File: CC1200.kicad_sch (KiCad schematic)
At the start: 36 parts, among them P1 AntMount, U3 CC1200, X1 40MHz

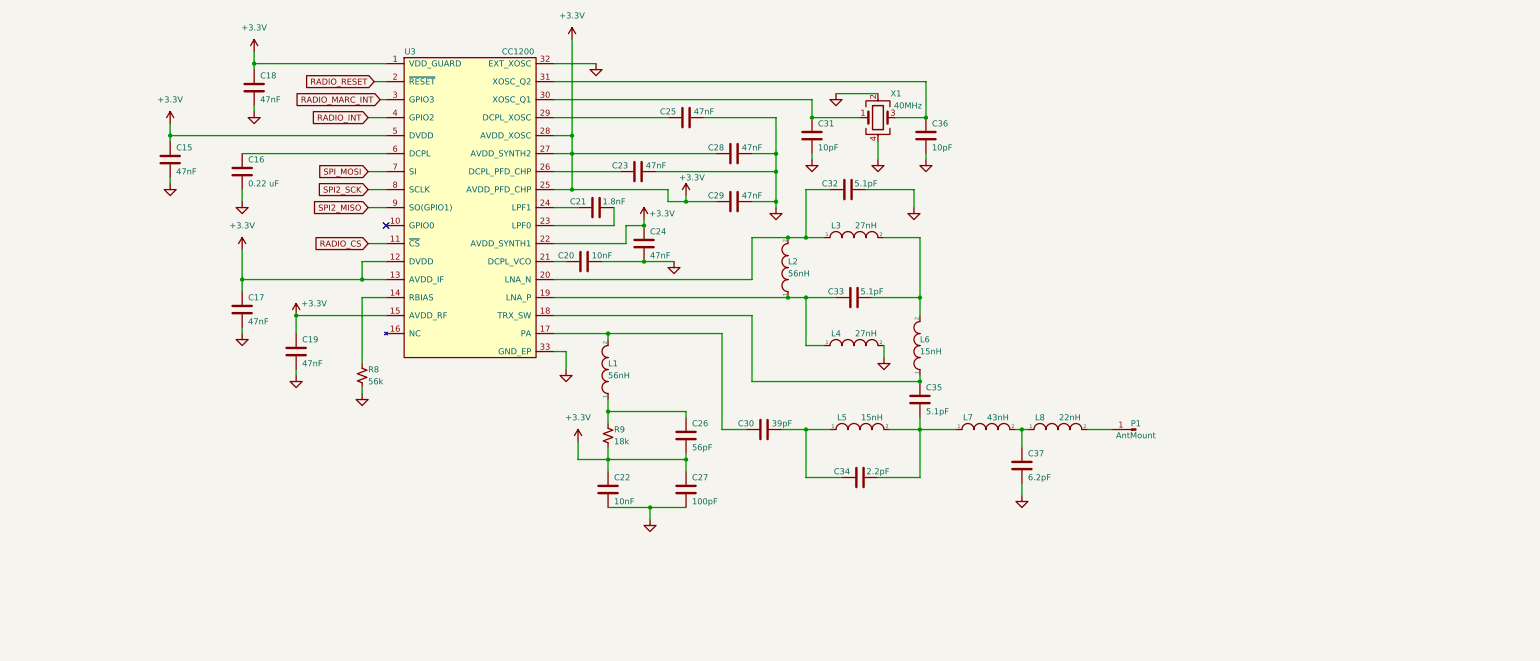
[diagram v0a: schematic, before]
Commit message: V4 Changes Added SKYWORKS +30db 4W FEM Added LM2576 3.9V supply Increased diameter to 60mm Re-routed full board
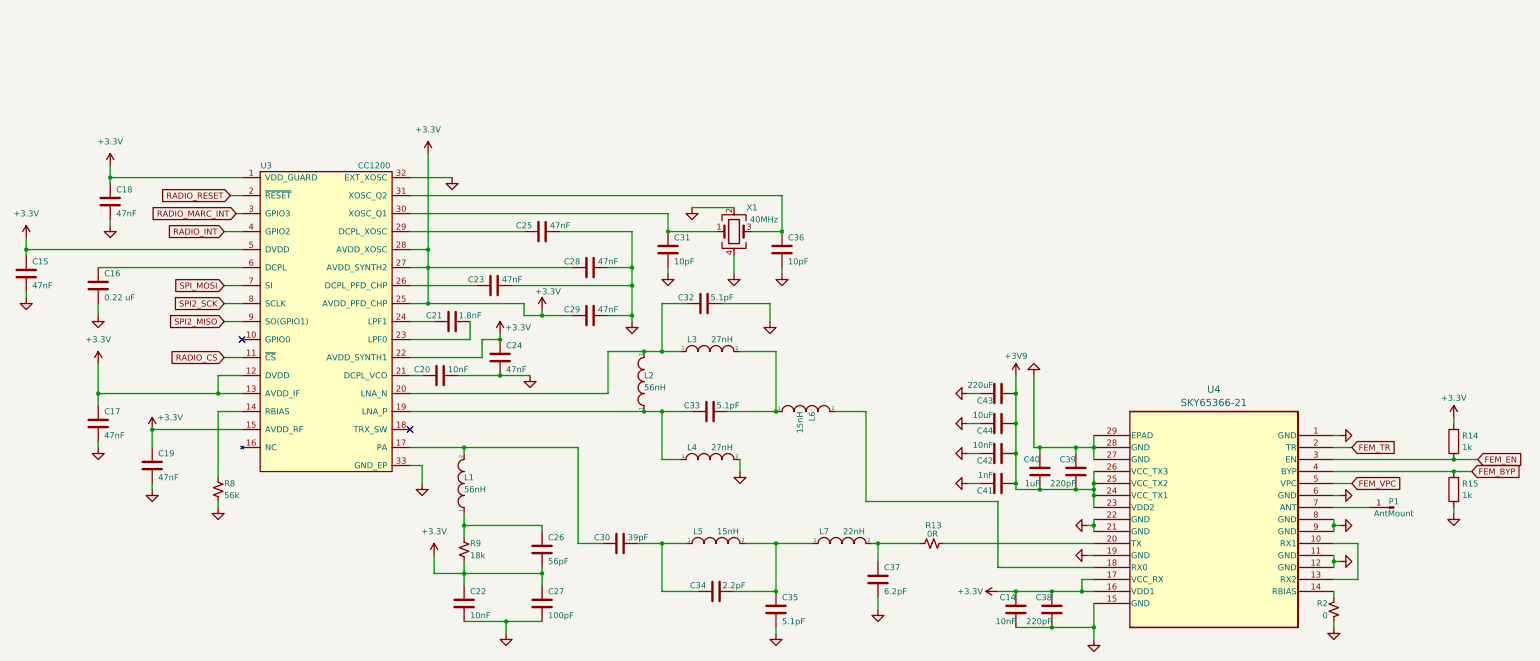
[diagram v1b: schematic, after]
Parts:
- removed L8: 22nH, Capacitor_SMD:C_0402_1005Metric, symbol pspice:INDUCTOR
- added C14, C42: 10nF, Capacitor_SMD:C_0402_1005Metric, symbol Device:C
- added C38, C39: 220pF, Capacitor_SMD:C_0402_1005Metric, symbol Device:C
- added C40: 1uF, Capacitor_SMD:C_0402_1005Metric, symbol Device:C
- added C41: 1nF, Capacitor_SMD:C_0402_1005Metric, symbol Device:C
- added C43: 220uF, Capacitor_SMD:C_1206_3216Metric, symbol Device:C
- added C44: 10uF, Capacitor_SMD:C_0402_1005Metric, symbol Device:C
- added R13: 0R, Capacitor_SMD:C_0402_1005Metric, symbol Device:R_Small_US
- added R14, R15: 1k, Resistor_SMD:R_0402_1005Metric, symbol Device:R
- added R2: 0, Capacitor_SMD:C_0402_1005Metric, symbol Device:R_Small_US
- added U4: SKY65366-21, SKY65366:SKY65366-21_SKY, symbol 2024-09-25_23-00-01:SKY65366-21
- L7: value 43nH -> 22nH; LCSC Part C2042359 -> C12670
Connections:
- net +3.3V: now also C14.1, C38.1, R14.2, U4.16 (VDD1), U4.17 (VCC_RX)
- net GND: now also C35.2, C14.2, C38.2, C39.1, C40.1, C41.1, C42.1, C43.1, C44.1, R15.1, R2.2, U4.1 (GND), U4.11 (GND), U4.12 (GND), U4.15 (GND), U4.19 (GND), U4.21 (GND), U4.22 (GND), U4.27 (GND), U4.28 (GND), U4.29 (EPAD), U4.6 (GND), U4.8 (GND), U4.9 (GND)
- net at C37.1, L7.2: now also R13.1
- net at P1.1 (Pin_1): now also U4.7 (ANT)
- net at C33.1, L3.2: now also L6.1; no longer L6.2
- net at C34.1, L5.2, L7.1: now also C35.1; no longer C35.2
- new net: R2.1, U4.14 (RBIAS)
- new net: R13.2, U4.20 (TX)
- new net: L6.2, U4.18 (RX0)
- new net: U4.10 (RX1), U4.13 (RX2)
- new net +3V9: C39.2, C40.2, C41.2, C42.2, C43.2, C44.2, U4.23 (VDD2), U4.24 (VCC_TX1), U4.25 (VCC_TX2), U4.26 (VCC_TX3)
- new net FEM_BYP: R15.2, U4.4 (BYP)
- new net FEM_EN: R14.1, U4.3 (EN)
- new net FEM_TR: U4.2 (TR)
- new net FEM_VPC: U4.5 (VPC)
- now unconnected: U3.18 (TRX_SW)
- no-connect marks 1 -> 2
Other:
- moved on the sheet: C15, C16, C17, C18, C19, C20, C21, C22, C23, C24, C25, C26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

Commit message: Adjusted some component footprints and part numbers Increased size of inductor and repositioned generated gbrs, drills, bom and cpl (up to date)
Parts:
- C21: LCSC Part C152808 -> C162192
- L1, L2: LCSC Part C76777 -> C167484
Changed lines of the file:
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@@
 			)
 		)
-		(property "LCSC Part" "C152808"
+		(property "LCSC Part" "C162192"
 			(at 109.22 101.6 0)
 			(effects
@@
 			)
 		)
-		(property "LCSC Part" "C76777"
+		(property "LCSC Part" "C167484"
 			(at 111.76 135.89 0)
 			(effects
@@
 			)
 		)
-		(property "LCSC Part" "C76777"
+		(property "LCSC Part" "C167484"
 			(at 149.86 114.3 0)
 			(effects

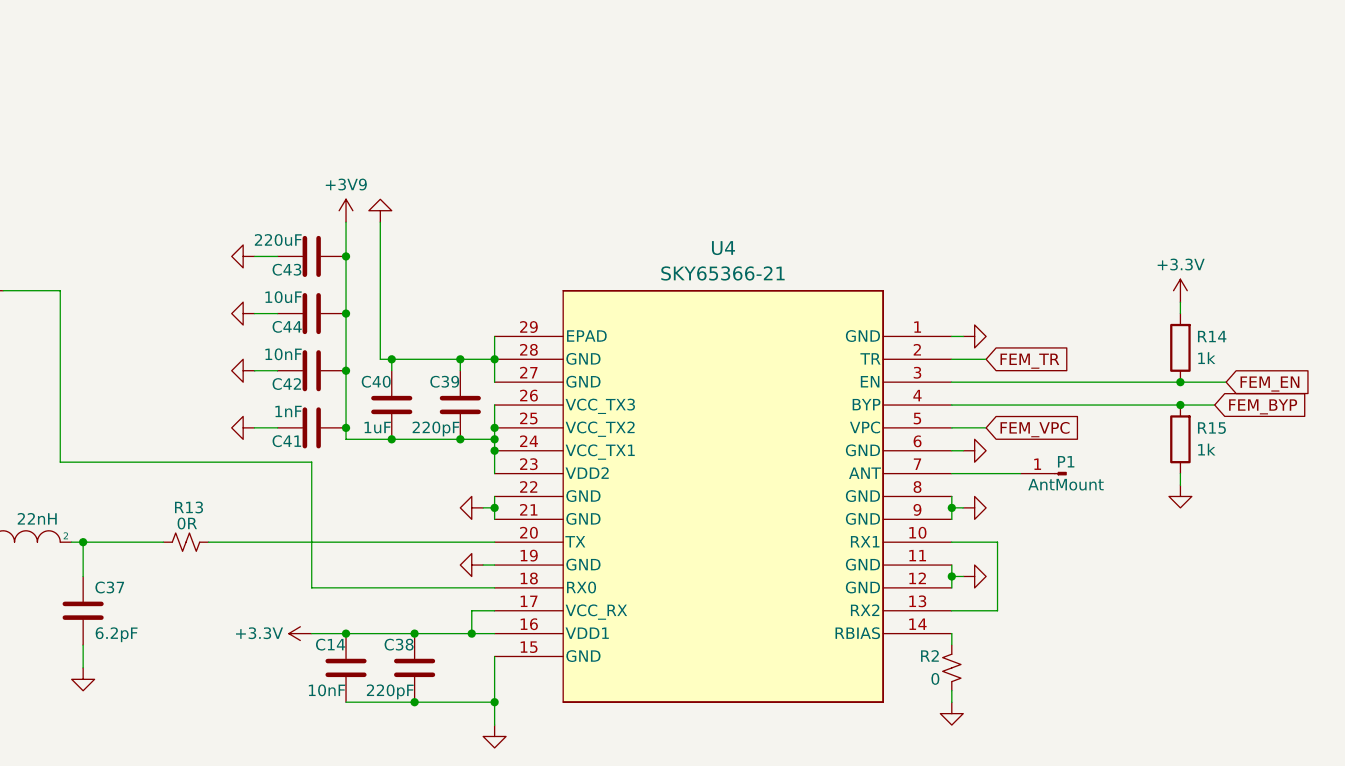
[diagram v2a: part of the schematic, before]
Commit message: removed old PA
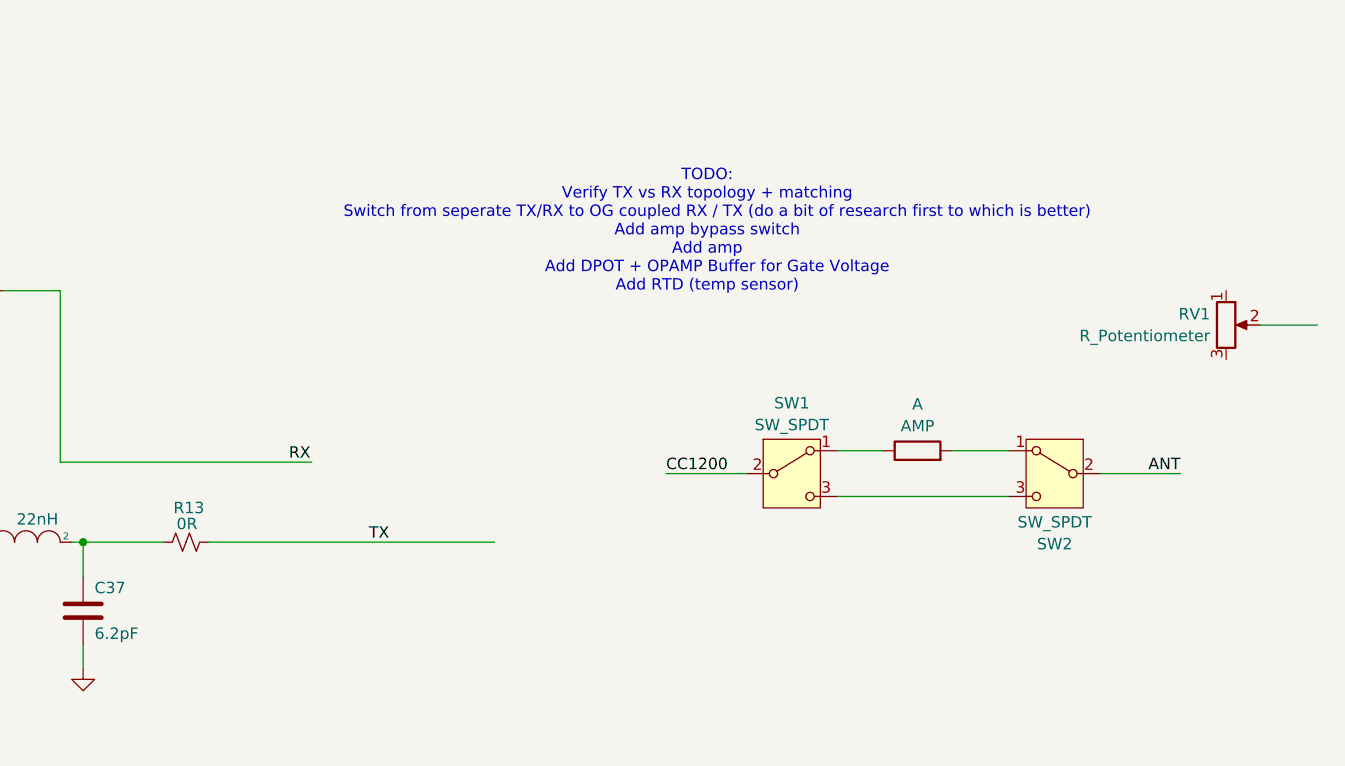
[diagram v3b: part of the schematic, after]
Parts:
- removed C14, C42: 10nF, Capacitor_SMD:C_0402_1005Metric, symbol Device:C
- removed C38, C39: 220pF, Capacitor_SMD:C_0402_1005Metric, symbol Device:C
- removed C40: 1uF, Capacitor_SMD:C_0402_1005Metric, symbol Device:C
- removed C41: 1nF, Capacitor_SMD:C_0402_1005Metric, symbol Device:C
- removed C43: 220uF, Capacitor_SMD:C_1206_3216Metric, symbol Device:C
- removed C44: 10uF, Capacitor_SMD:C_0402_1005Metric, symbol Device:C
- removed P1: AntMount, Connector_Coaxial:SMA_Amphenol_132134-11_Vertical, symbol Connector:Conn_01x01_Male
- removed R14, R15: 1k, Resistor_SMD:R_0402_1005Metric, symbol Device:R
- removed R2: 0, Capacitor_SMD:C_0402_1005Metric, symbol Device:R_Small_US
- removed U4: SKY65366-21, SKY65366:SKY65366-21_SKY, symbol 2024-09-25_23-00-01:SKY65366-21
- added A: AMP, symbol Device:R
- added RV1: R_Potentiometer, symbol Device:R_Potentiometer
- added SW1, SW2: SW_SPDT, symbol Switch:SW_SPDT
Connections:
- net TX: now reaches R13.2
- net RX: now reaches L6.2
- new net: A.1, SW1.1 (A)
- new net: SW1.3 (C), SW2.3 (C)
- new net: A.2, SW2.1 (A)
- new net ANT: SW2.2 (B)
- new net CC1200: SW1.2 (B)
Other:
- note added: "TODO: Verify TX vs RX topology + matching Switch from seperate TX/RX to OG coupled RX / TX (do a bit of research first to which is better) Add amp bypass switch Add amp Add DPOT + OPAMP Buffer for Gate Voltage Add RTD (temp sensor)"

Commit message: added Mitsibushi Amp w/ supporting gate control circuitry, switching, and temperature monitoring
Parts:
- removed A: AMP, symbol Device:R
- removed RV1: R_Potentiometer, symbol Device:R_Potentiometer
- removed SW1, SW2: SW_SPDT, symbol Switch:SW_SPDT
- added AE2: Antenna_Shield, Connector_Coaxial:SMA_Amphenol_132134-11_Vertical, symbol Device:Antenna_Shield
- added C67, C70, C71: 0.1uF, Capacitor_SMD:C_0402_1005Metric, symbol Device:C
- added C68, C72, C73: 100pF, Capacitor_SMD:C_0402_1005Metric, symbol Device:C
- added C69: 10nF, Capacitor_SMD:C_0402_1005Metric, symbol Device:C
- added JP3: SolderJumper_2_Bridged, Jumper:SolderJumper-2_P1.3mm_Bridged_RoundedPad1.0x1.5mm, symbol Jumper:SolderJumper_2_Bridged
- added JP4: SolderJumper_2_Open, Jumper:SolderJumper-2_P1.3mm_Open_RoundedPad1.0x1.5mm, symbol Jumper:SolderJumper_2_Open
- added L16: 43nH, Inductor_SMD:L_0402_1005Metric, symbol pspice:INDUCTOR
- added PE4259-63: 4259-63, Package_TO_SOT_SMD:SOT-363_SC-70-6, symbol 4259-63:4259-63
- added R17: 100, Resistor_SMD:R_0402_1005Metric, symbol Device:R_US
- added R18: 1000, Resistor_SMD:R_0402_1005Metric, symbol Device:R_US
- added R19: 1k, Resistor_SMD:R_0402_1005Metric, symbol Device:R_Small_US
- added RFAMP2: RA07H4047M-101, RA07H4047m:RA07h4047M, symbol RA07H4047M-101:RA07H4047M-101
- added TH1: PT100, Resistor_SMD:R_0603_1608Metric, symbol Sensor_Temperature:PT100
- added U7: MCP41010, MCP41010:SOIC127P599X175-8N, symbol Potentiometer_Digital:MCP41010
- added U8: MCP6001-OT, Package_TO_SOT_SMD:SOT-23-5, symbol Amplifier_Operational:MCP6001-OT
- R9: value 18k -> 18; footprint Capacitor_SMD:C_0402_1005Metric -> Resistor_SMD:R_0402_1005Metric
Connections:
- net RX is gone; now on an unnamed net: L6.2
- net +3.3V: now also C70.2, C71.1, PE4259-63.6 (~{CTRL_OR_VDD}), R19.2, TH1.2, U7.5 (PA0), U7.8 (VDD), U8.5 (V+)
- net GND: now also AE2.2 (Shield), C67.2, C69.1, C70.1, C71.2, PE4259-63.2 (GND), R17.2, RFAMP2.5 (GND), U7.4 (VSS), U7.7 (PB0), U8.2 (V-); no longer C35.2
- net at U3.18 (TRX_SW): now also C35.1
- net at C34.1, L5.2: now also C35.2, L16.2; no longer C35.1, L7.1
- net at L7.2, R13.1: no longer C37.1
- net TX: no longer names the net of R13.2
- net TX: now also C68.1
- new net: AE2.1 (A), C73.2, RFAMP2.4 (RF_OUTPUT_(POUT))
- new net: JP3.1 (A), U7.6 (PW0)
- new net: JP3.2 (B), JP4.1 (A), U8.3 (+)
- new net: R17.1, R18.1, TH1.1
- new net: C73.1, PE4259-63.1 (RF1)
- new net: C72.1, PE4259-63.3 (RF2)
- new net: C68.2, PE4259-63.5 (RFC)
- new net: C72.2, RFAMP2.1 (RF_INPUT_(PIN))
- new net: C37.1, L16.1, L7.1
- new net: RFAMP2.2 (GATE_VOLTAGE_(VGG)), U8.1, U8.4 (-)
- new net +BATT: RFAMP2.3 (DRAIN_VOLTAGE_(VDD))
- new net AMP_ON: JP4.2 (B)
- new net AMP_SW_CTRL: C69.2, PE4259-63.4 (CTRL), R19.1
- new net DPOT_CS: U7.1 (~{CS})
- new net DPOT_MOSI: U7.3 (SI)
- new net DPOT_SCLK: U7.2 (SCK)
- new net TEMPSENSORADC: C67.1, R18.2
- no-connect marks 2 -> 1
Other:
- note added: "TEMPERATURE SENSING"
- note removed: "TODO: Verify TX vs RX topology + matching Switch from seperate TX/RX to OG coupled RX / TX (do a bit of research first to which is better) Add amp bypass switch Add amp Add DPOT + OPAMP Buffer for Gate Voltage Add RTD (temp sensor)"
- moved on the sheet: L6, L7, R13

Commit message: BOM fixes and manufactureing files
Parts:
- AE2: LCSC C496549 -> (none); LCSC Part (none) -> C496549
- C67, C71: LCSC C1525 -> (none); LCSC Part (none) -> C1525
- L16: LCSC C167478 -> (none); LCSC Part (none) -> C167478
- PE4259-63: LCSC C470892 -> (none); LCSC Part (none) -> C470892
- R17: LCSC C25076 -> (none); LCSC Part (none) -> C25076
- R18: LCSC C21190 -> (none); LCSC Part (none) -> C21190
- TH1: LCSC C141518 -> (none); LCSC Part (none) -> C141518
- U7: LCSC C136395 -> (none); LCSC Part (none) -> C136395
- U8: LCSC Part (none) -> C116490
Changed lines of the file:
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@@
 			)
 		)
-		(property "LCSC" "C496549"
+		(property "LCSC Part" "C496549"
 			(at 387.35 165.1 90)
 			(effects
@@
 			)
 		)
-		(property "LCSC" "C21190"
+		(property "LCSC Part" "C21190"
 			(at 368.3 38.1 0)
 			(effects
@@
 			)
 		)
-		(property "LCSC" "C470892"
+		(property "LCSC Part" "C470892"
 			(at 318.77 153.67 0)
 			(effects
@@
 			)
 		)
-		(property "LCSC" "C167478"
+		(property "LCSC Part" "C167478"
 			(at 189.23 148.59 0)
 			(effects
@@
 			)
 		)
-		(property "LCSC" "C136395"
+		(property "LCSC Part" "C136395"
 			(at 293.37 99.06 0)
 			(effects
@@
 			)
 		)
-		(property "LCSC" "C1525"
+		(property "LCSC Part" "C1525"
 			(at 307.34 88.9 0)
 			(effects
@@
 			)
 		)
+		(property "LCSC Part" "C116490"
+			(at 335.28 110.49 0)
+			(effects
+				(font
+					(size 1.27 1.27)
+				)
+				(hide yes)
+			)
+		)
 		(pin "4"
 		)
@@
 			)
 		)
-		(property "LCSC" "C25076"
+		(property "LCSC Part" "C25076"
 			(at 355.6 44.45 0)
 			(effects
@@
 			)
 		)
-		(property "LCSC" "C1525"
+		(property "LCSC Part" "C1525"
 			(at 374.65 44.45 0)
 			(effects
@@
 			)
 		)
-		(property "LCSC" "C141518"
+		(property "LCSC Part" "C141518"
 			(at 355.6 31.75 0)
 			(effects
